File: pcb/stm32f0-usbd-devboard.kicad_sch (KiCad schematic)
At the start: 23 parts, among them J1 USB_B_Mini, J2 PIN H 5P, J3 LEFT, J4 RIGHT, U1 USBLC6-2SC6, U2 MCP1700-3302E, U3 STM32F042K4T6 or STM32F042K6T6

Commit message: pcb: revision 20241212
new protoboard-friendly pcb revision.
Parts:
- J3: footprint custom:PinHeader_DevBoard_Connector_1x12_P2.54mm_Vertical -> custom:PinHeader_DevBoard_Left_Connector_1x12_P2.54mm_Vertical
- J4: footprint custom:PinHeader_DevBoard_Connector_1x12_P2.54mm_Vertical -> custom:PinHeader_DevBoard_Right_Connector_1x12_P2.54mm_Vertical
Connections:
- net GND: now also J3.1 (Pin_1), J4.1 (Pin_1); no longer J3.2 (Pin_2), J4.2 (Pin_2)
- net +3.3V renamed 3.3V
- net 3.3V: now also J3.2 (Pin_2); no longer J3.1 (Pin_1)
- net +5V renamed 5V
- net 5V: now also J4.2 (Pin_2); no longer J4.1 (Pin_1)
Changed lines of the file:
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@@
 	(title_block
 		(title "stm32f0-usbd-devboard")
-		(date "2024-12-10")
-		(rev "20241210")
+		(date "2024-12-12")
+		(rev "20241212")
 		(comment 3 "Released under CERN Open Hardware Licence Version 2 - Strongly Reciprocal")
 		(comment 4 "Designed by: Rafael G. Martins")
@@
 	(wire
 		(pts
-			(xy 222.25 76.2) (xy 222.25 74.93)
+			(xy 219.71 74.93) (xy 219.71 78.74)
 		)
 		(stroke
@@
 	(wire
 		(pts
-			(xy 245.11 78.74) (xy 242.57 78.74)
+			(xy 245.11 76.2) (xy 245.11 107.95)
 		)
 		(stroke
@@
 	(wire
 		(pts
-			(xy 245.11 107.95) (xy 245.11 78.74)
+			(xy 182.88 105.41) (xy 184.15 105.41)
 		)
 		(stroke
@@
 	(wire
 		(pts
-			(xy 182.88 105.41) (xy 184.15 105.41)
+			(xy 146.05 185.42) (xy 147.32 185.42)
 		)
 		(stroke
@@
 	(wire
 		(pts
-			(xy 146.05 185.42) (xy 147.32 185.42)
+			(xy 151.765 112.395) (xy 151.765 113.665)
 		)
 		(stroke
@@
 	(wire
 		(pts
-			(xy 151.765 112.395) (xy 151.765 113.665)
+			(xy 219.71 78.74) (xy 224.79 78.74)
 		)
 		(stroke
@@
 	(wire
 		(pts
+			(xy 222.25 76.2) (xy 222.25 107.95)
+		)
+		(stroke
+			(width 0)
+			(type default)
+		)
+	)
+	(wire
+		(pts
 			(xy 220.98 83.82) (xy 224.79 83.82)
 		)
@@
 	(wire
 		(pts
-			(xy 224.79 76.2) (xy 222.25 76.2)
-		)
-		(stroke
-			(width 0)
-			(type default)
-		)
-	)
-	(wire
-		(pts
 			(xy 161.29 67.31) (xy 161.29 64.77)
 		)
@@
 	(wire
 		(pts
-			(xy 245.11 76.2) (xy 245.11 74.93)
+			(xy 222.25 76.2) (xy 224.79 76.2)
+		)
+		(stroke
+			(width 0)
+			(type default)
+		)
+	)
+	(wire
+		(pts
+			(xy 247.65 74.93) (xy 247.65 78.74)
 		)
 		(stroke
@@
 	(wire
 		(pts
+			(xy 242.57 78.74) (xy 247.65 78.74)
+		)
+		(stroke
+			(width 0)
+			(type default)
+		)
+	)
+	(wire
+		(pts
 			(xy 242.57 91.44) (xy 246.38 91.44)
 		)
@@
 	(wire
 		(pts
-			(xy 222.25 107.95) (xy 222.25 78.74)
-		)
-		(stroke
-			(width 0)
-			(type default)
-		)
-	)
-	(wire
-		(pts
 			(xy 50.8 128.905) (xy 52.07 128.905)
 		)
@@
 	(wire
 		(pts
+			(xy 245.11 76.2) (xy 242.57 76.2)
+		)
+		(stroke
+			(width 0)
+			(type default)
+		)
+	)
+	(wire
+		(pts
 			(xy 62.865 97.79) (xy 74.93 97.79)
 		)
@@
 	(wire
 		(pts
-			(xy 242.57 76.2) (xy 245.11 76.2)
-		)
-		(stroke
-			(width 0)
-			(type default)
-		)
-	)
-	(wire
-		(pts
 			(xy 220.98 93.98) (xy 224.79 93.98)
 		)
@@
 	(wire
 		(pts
-			(xy 222.25 78.74) (xy 224.79 78.74)
-		)
-		(stroke
-			(width 0)
-			(type default)
-		)
-	)
-	(wire
-		(pts
 			(xy 62.865 88.9) (xy 62.865 90.805)
 		)
@@
 			)
 		)
-		(property "Footprint" "custom:PinHeader_DevBoard_Connector_1x12_P2.54mm_Vertical"
+		(property "Footprint" "custom:PinHeader_DevBoard_Right_Connector_1x12_P2.54mm_Vertical"
 			(at 237.49 88.9 0)
 			(effects
@@
 			)
 		)
-		(property "Value" "+5V"
-			(at 69.215 36.195 0)
+		(property "Value" "5V"
+			(at 69.215 36.83 0)
 			(effects
 				(font
@@
 			)
 		)
-		(property "Value" "+3.3V"
+		(property "Value" "3.3V"
 			(at 56.515 116.84 0)
 			(effects
@@
 	(symbol
 		(lib_id "power:+3.3V")
-		(at 222.25 74.93 0)
+		(at 219.71 74.93 0)
 		(unit 1)
 		(exclude_from_sim no)
@@
 		(fields_autoplaced yes)
 		(property "Reference" "#PWR020"
-			(at 222.25 78.74 0)
+			(at 219.71 78.74 0)
 			(effects
 				(font
@@
 			)
 		)
-		(property "Value" "+3.3V"
-			(at 222.25 69.85 0)
+		(property "Value" "3.3V"
+			(at 219.71 69.85 0)
 			(effects
 				(font
@@
 		)
 		(property "Footprint" ""
-			(at 222.25 74.93 0)
+			(at 219.71 74.93 0)
 			(effects
 				(font
@@
 		)
 		(property "Datasheet" ""
-			(at 222.25 74.93 0)
+			(at 219.71 74.93 0)
 			(effects
 				(font
@@
 		)
 		(property "Description" "Power symbol creates a global label with name \"+3.3V\""
-			(at 222.25 74.93 0)
+			(at 219.71 74.93 0)
 			(effects
 				(font
@@
 	(symbol
 		(lib_id "power:+5V")
-		(at 245.11 74.93 0)
+		(at 247.65 74.93 0)
 		(unit 1)
 		(exclude_from_sim no)
@@
 		(fields_autoplaced yes)
 		(property "Reference" "#PWR021"
-			(at 245.11 78.74 0)
+			(at 247.65 78.74 0)
 			(effects
 				(font
@@
 			)
 		)
-		(property "Value" "+5V"
-			(at 245.11 69.85 0)
+		(property "Value" "5V"
+			(at 247.65 69.85 0)
 			(effects
 				(font
@@
 		)
 		(property "Footprint" ""
-			(at 245.11 74.93 0)
+			(at 247.65 74.93 0)
 			(effects
 				(font
@@
 		)
 		(property "Datasheet" ""
-			(at 245.11 74.93 0)
+			(at 247.65 74.93 0)
 			(effects
 				(font
@@
 		)
 		(property "Description" "Power symbol creates a global label with name \"+5V\""
-			(at 245.11 74.93 0)
+			(at 247.65 74.93 0)
 			(effects
 				(font
@@
 			)
 		)
-		(property "Value" "+3.3V"
+		(property "Value" "3.3V"
 			(at 170.18 50.8 0)
 			(effects
@@
 			)
 		)
-		(property "Footprint" "custom:PinHeader_DevBoard_Connector_1x12_P2.54mm_Vertical"
+		(property "Footprint" "custom:PinHeader_DevBoard_Left_Connector_1x12_P2.54mm_Vertical"
 			(at 229.87 88.9 0)
 			(effects
@@
 			)
 		)
-		(property "Value" "+3.3V"
-			(at 86.995 81.915 0)
+		(property "Value" "3.3V"
+			(at 86.995 82.55 0)
 			(effects
 				(font
@@
 			)
 		)
-		(property "Value" "+5V"
-			(at 62.865 81.915 0)
+		(property "Value" "5V"
+			(at 62.865 82.55 0)
 			(effects
 				(font
@@
 			)
 		)
-		(property "Value" "+3.3V"
-			(at 129.54 105.41 90)
+		(property "Value" "3.3V"
+			(at 129.54 105.4099 90)
 			(effects
 				(font
@@
 			)
 		)
-		(property "Value" "+5V"
+		(property "Value" "5V"
 			(at 89.535 36.83 0)
 			(effects

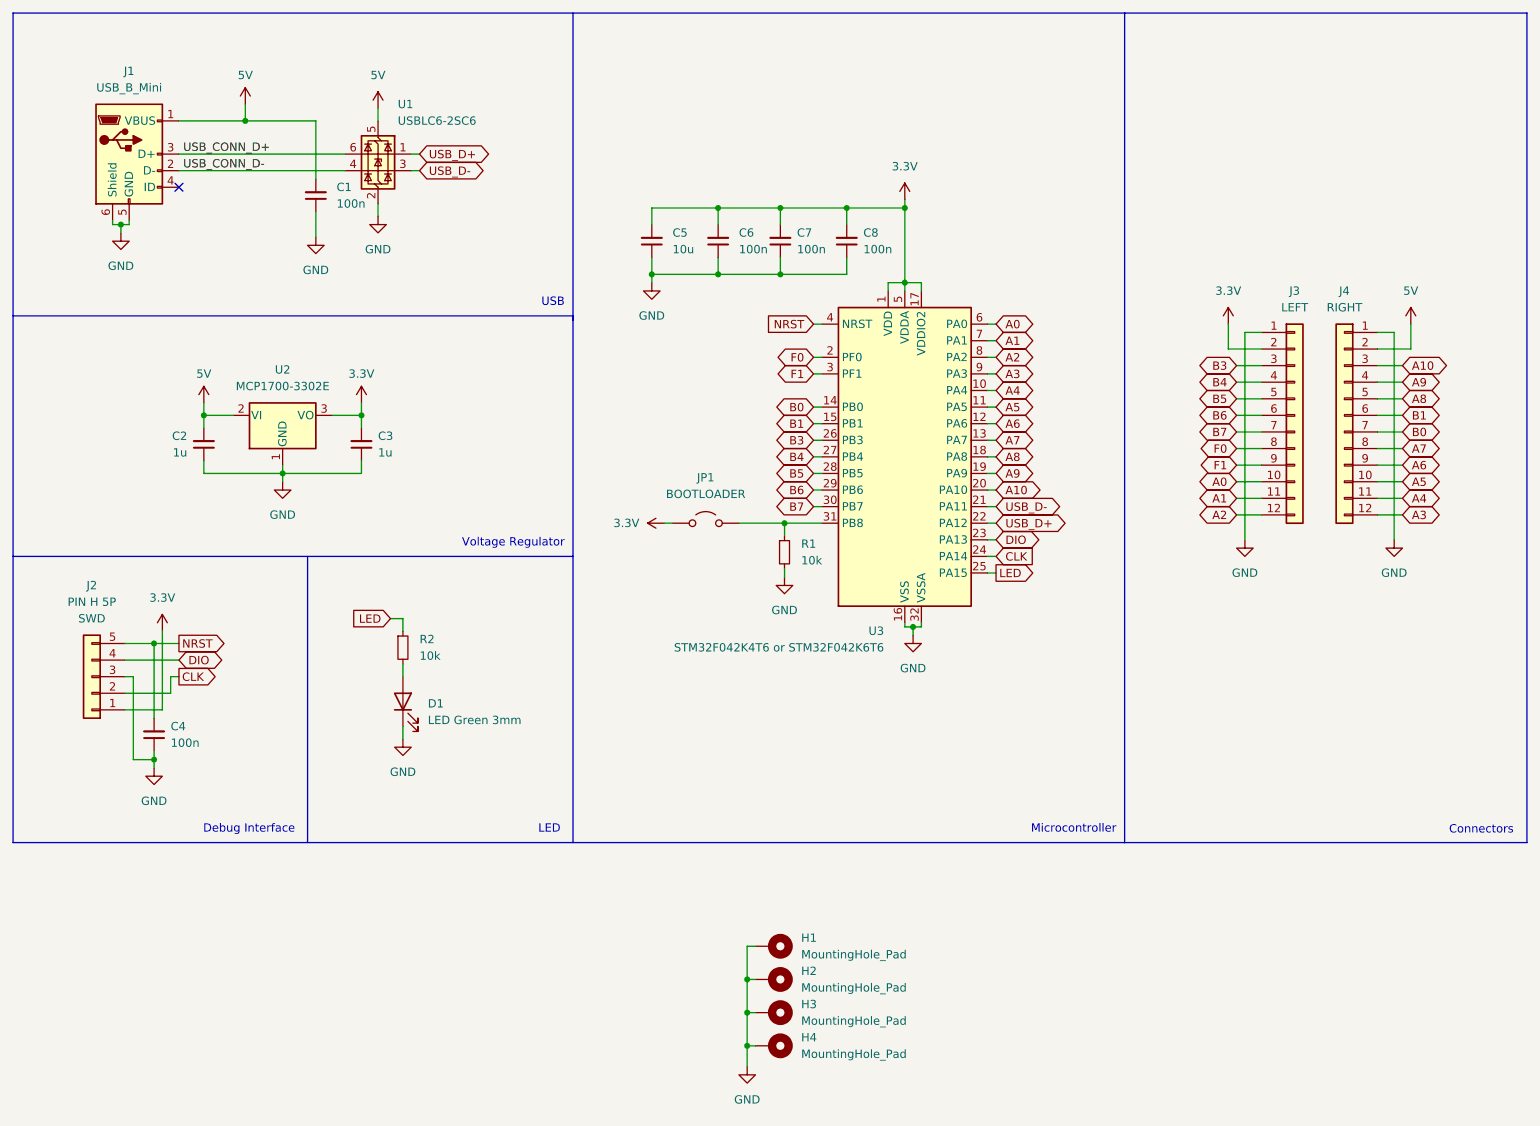
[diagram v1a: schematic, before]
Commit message: pcb: upgrade to kicad 9
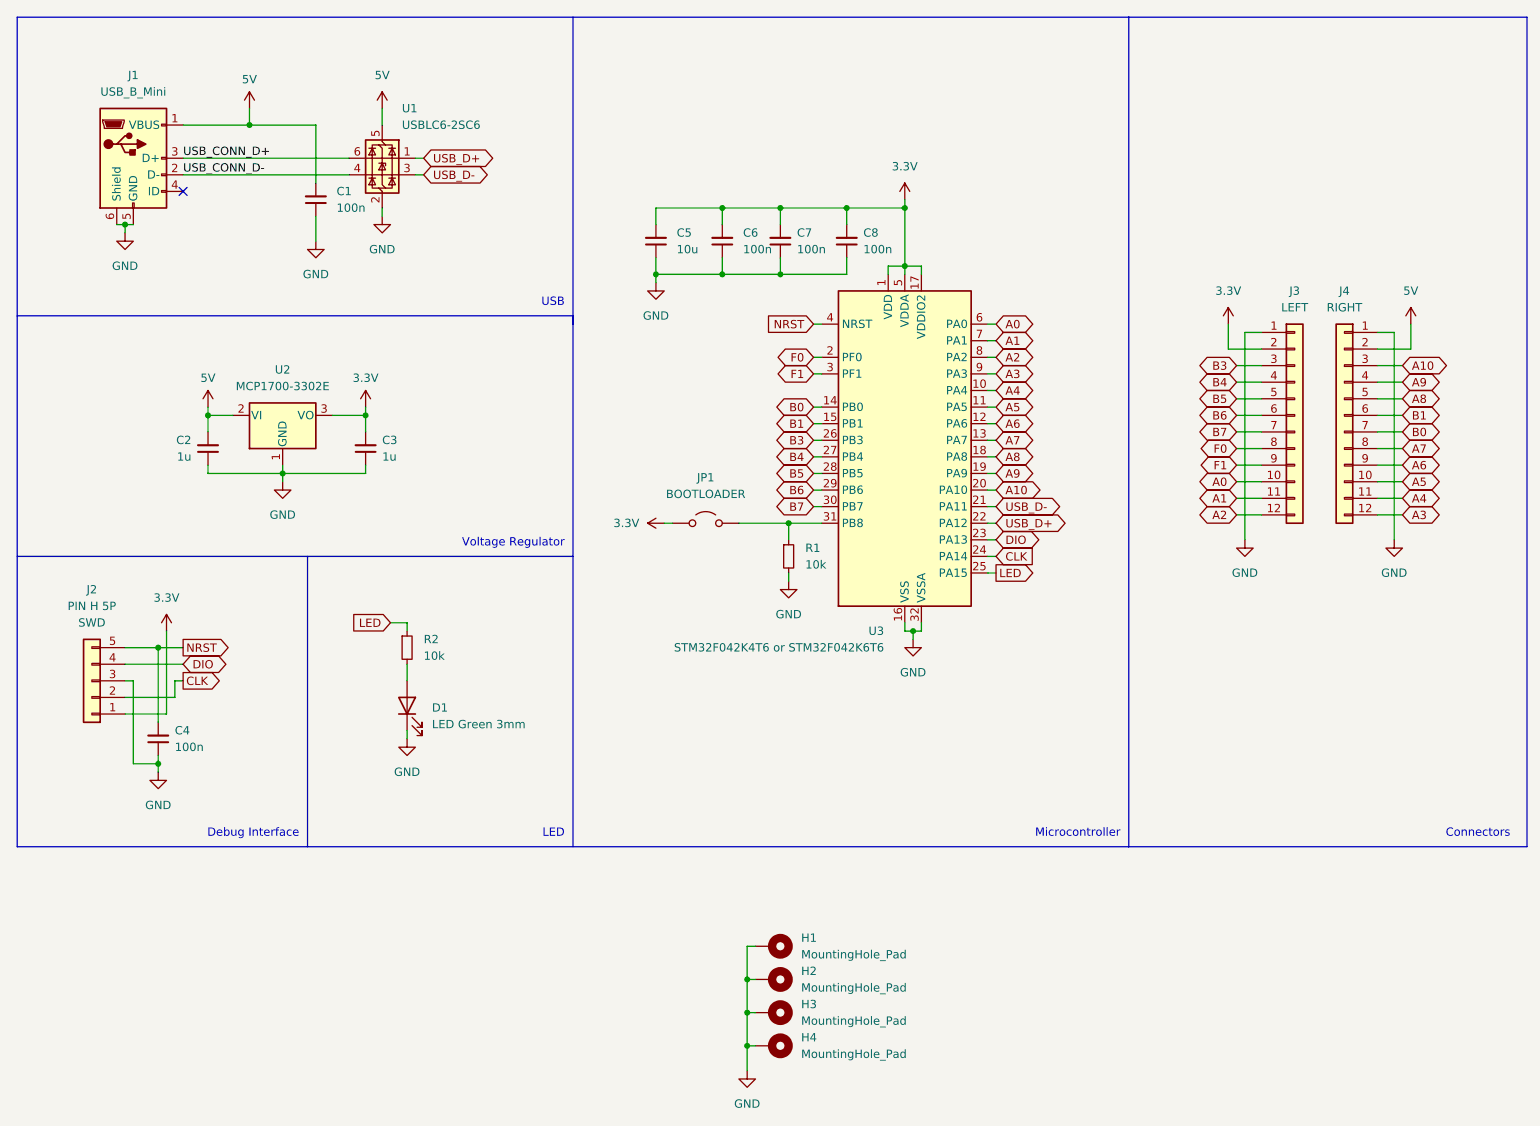
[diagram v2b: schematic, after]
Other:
- moved on the sheet: C1, C2, C3, C4, C5, C6, D1, J1, J2, R1, R2, U1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
